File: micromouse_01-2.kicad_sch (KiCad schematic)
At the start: 41 parts, among them IC3 ADS7066IRTER, IC4 PCA9632TK,118, J2 Fan+, J3 Fan-, J4 Battery, J5 Battery, Q1 SiA910, Q9 SSM6J808R_LXHF, SW1 SSSS810701, U4 SMT-0440-S-R, U5 WS2812-2020, U7 LXDC55FAAA-203

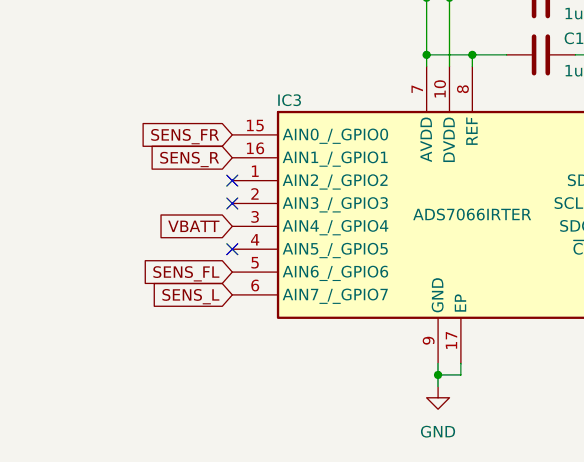
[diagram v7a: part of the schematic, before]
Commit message: Added 3D model
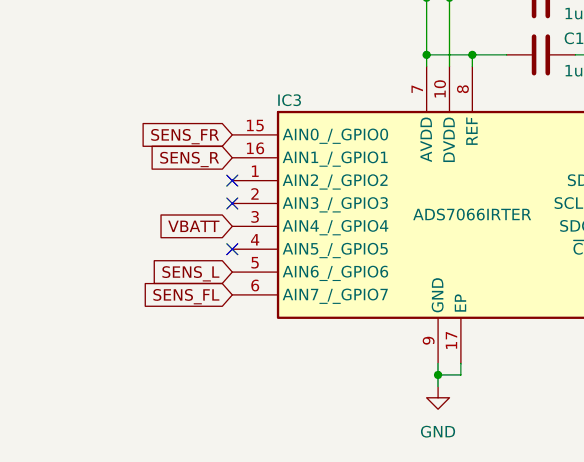
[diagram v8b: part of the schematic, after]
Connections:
- net SENS_FL: now also IC3.6 (AIN7_/_GPIO7); no longer IC3.5 (AIN6_/_GPIO6)
- net SENS_L: now also IC3.5 (AIN6_/_GPIO6); no longer IC3.6 (AIN7_/_GPIO7)
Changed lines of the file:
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@@
+    )
+  )
+  (global_label "SENS_FL" (shape input) (at 44.45 161.29 180) (fields_autoplaced)
+    (effects (font (size 1.27 1.27)) (justify right))
+    (property "Intersheetrefs" "${INTERSHEET_REFS}" (at 33.482 161.29 0)
+      (effects (font (size 1.27 1.27)) (justify right) hide)
     )
   )
@@
     (effects (font (size 1.27 1.27)) (justify right))
     (property "Intersheetrefs" "${INTERSHEET_REFS}" (at 33.2401 143.51 0)
+      (effects (font (size 1.27 1.27)) (justify right) hide)
+    )
+  )
+  (global_label "SENS_L" (shape input) (at 44.45 158.75 180) (fields_autoplaced)
+    (effects (font (size 1.27 1.27)) (justify right))
+    (property "Intersheetrefs" "${INTERSHEET_REFS}" (at 34.5706 158.75 0)
       (effects (font (size 1.27 1.27)) (justify right) hide)
     )
@@
     )
   )
-  (global_label "SENS_L" (shape input) (at 44.45 161.29 180) (fields_autoplaced)
-    (effects (font (size 1.27 1.27)) (justify right))
-    (property "Intersheetrefs" "${INTERSHEET_REFS}" (at 34.5706 161.29 0)
-      (effects (font (size 1.27 1.27)) (justify right) hide)
-    )
-  )
   (global_label "SENS_FL" (shape output) (at 48.26 35.56 0) (fields_autoplaced)
     (effects (font (size 1.27 1.27)) (justify left))
@@
       (effects (font (size 1.27 1.27)) (justify right) hide)
     )
-  )
-  (global_label "SENS_FL" (shape input) (at 44.45 158.75 180) (fields_autoplaced)
-    (effects (font (size 1.27 1.27)) (justify right))
-    (property "Intersheetrefs" "${INTERSHEET_REFS}" (at 33.482 158.75 0)
-      (effects (font (size 1.27 1.27)) (justify right) hide)
-    )
